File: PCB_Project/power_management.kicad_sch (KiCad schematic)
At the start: 0 parts

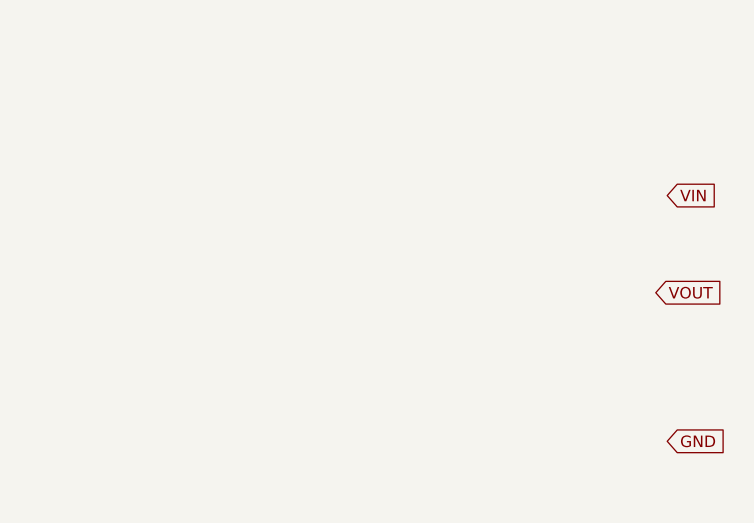
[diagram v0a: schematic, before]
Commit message: added power board
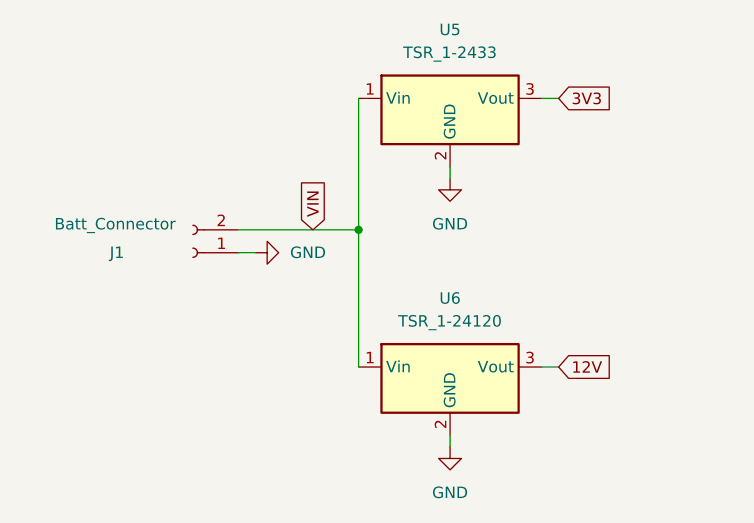
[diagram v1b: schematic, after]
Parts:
- added J1: Batt_Connector, symbol Connector:Conn_01x02_Socket
- added U5: TSR_1-2433, Converter_DCDC:Converter_DCDC_TRACO_TSR-1_THT, symbol Regulator_Switching:TSR_1-2433
- added U6: TSR_1-24120, Converter_DCDC:Converter_DCDC_TRACO_TSR-1_THT, symbol Regulator_Switching:TSR_1-24120
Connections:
- net GND: now also J1.1 (Pin_1), U5.2 (GND), U6.2 (GND)
- net VIN: now also J1.2 (Pin_2), U5.1 (Vin), U6.1 (Vin)
- new net 12V: U6.3 (Vout)
- new net 3V3: U5.3 (Vout)
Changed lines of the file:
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@@
 (kicad_sch (version 20230121) (generator eeschema)
   (paper "A4")
-  (global_label "VIN" (shape input) (at 144.145 64.135 0) (fields_autoplaced)
+  (junction (at 109.855 67.945) (diameter 0) (color 0 0 0 0)
+  )
+  (wire (pts (xy 120.015 60.96) (xy 120.015 62.23))
+    (stroke (width 0) (type default))
+  )
+  (wire (pts (xy 96.52 70.485) (xy 98.425 70.485))
+    (stroke (width 0) (type default))
+  )
+  (wire (pts (xy 96.52 67.945) (xy 109.855 67.945))
+    (stroke (width 0) (type default))
+  )
+  (wire (pts (xy 120.015 90.805) (xy 120.015 92.075))
+    (stroke (width 0) (type default))
+  )
+  (wire (pts (xy 130.175 53.34) (xy 132.08 53.34))
+    (stroke (width 0) (type default))
+  )
+  (wire (pts (xy 109.855 67.945) (xy 109.855 83.185))
+    (stroke (width 0) (type default))
+  )
+  (wire (pts (xy 130.175 83.185) (xy 132.08 83.185))
+    (stroke (width 0) (type default))
+  )
+  (wire (pts (xy 109.855 67.945) (xy 109.855 53.34))
+    (stroke (width 0) (type default))
+  )
+  (global_label "3V3" (shape input) (at 132.08 53.34 0) (fields_autoplaced)
     (effects (font (size 1.27 1.27)) (justify left))
-    (property "Intersheetrefs" "${INTERSHEET_REFS}" (at 150.0747 64.135 0)
+    (property "Intersheetrefs" "${INTERSHEET_REFS}" (at 138.4934 53.34 0)
       (effects (font (size 1.27 1.27)) (justify left) hide)
     )
   )
-  (global_label "GND" (shape input) (at 144.145 91.44 0) (fields_autoplaced)
+  (global_label "VIN" (shape input) (at 104.775 67.945 90) (fields_autoplaced)
     (effects (font (size 1.27 1.27)) (justify left))
-    (property "Intersheetrefs" "${INTERSHEET_REFS}" (at 150.9213 91.44 0)
+    (property "Intersheetrefs" "${INTERSHEET_REFS}" (at 104.775 62.0153 90)
       (effects (font (size 1.27 1.27)) (justify left) hide)
     )
   )
-  (global_label "VOUT" (shape input) (at 142.875 74.93 0) (fields_autoplaced)
+  (global_label "12V" (shape input) (at 132.08 83.185 0) (fields_autoplaced)
     (effects (font (size 1.27 1.27)) (justify left))
-    (property "Intersheetrefs" "${INTERSHEET_REFS}" (at 150.498 74.93 0)
+    (property "Intersheetrefs" "${INTERSHEET_REFS}" (at 138.4934 83.185 0)
       (effects (font (size 1.27 1.27)) (justify left) hide)
     )
   )
+  (symbol (lib_id "Regulator_Switching:TSR_1-24120") (at 120.015 85.725 0) (unit 1)
+    (in_bom yes) (on_board yes) (dnp no)
+    (property "Reference" "U6" (at 120.015 75.565 0)
+      (effects (font (size 1.27 1.27)))
+    )
+    (property "Value" "TSR_1-24120" (at 120.015 78.105 0)
+      (effects (font (size 1.27 1.27)))
+    )
+    (property "Footprint" "Converter_DCDC:Converter_DCDC_TRACO_TSR-1_THT" (at 120.015 89.535 0)
+      (effects (font (size 1.27 1.27) italic) (justify left) hide)
+    )
+    (property "Datasheet" "http://www.tracopower.com/products/tsr1.pdf" (at 120.015 85.725 0)
+      (effects (font (size 1.27 1.27)) hide)
+    )
+    (pin "1")
+    (pin "2")
+    (pin "3")
+    (instances
+      (project "PCB_Project"
+        (path "/3dbd20c6-0b48-4a74-89bd-dd4c54711bfb/c1270458-3028-4230-aa43-c8411af46874"
+          (reference "U6") (unit 1)
+        )
+      )
+    )
+  )
+  (symbol (lib_id "Regulator_Switching:TSR_1-2433") (at 120.015 55.88 0) (unit 1)
+    (in_bom yes) (on_board yes) (dnp no) (fields_autoplaced)
+    (property "Reference" "U5" (at 120.015 45.72 0)
+      (effects (font (size 1.27 1.27)))
+    )
+    (property "Value" "TSR_1-2433" (at 120.015 48.26 0)
+      (effects (font (size 1.27 1.27)))
+    )
+    (property "Footprint" "Converter_DCDC:Converter_DCDC_TRACO_TSR-1_THT" (at 120.015 59.69 0)
+      (effects (font (size 1.27 1.27) italic) (justify left) hide)
+    )
+    (property "Datasheet" "http://www.tracopower.com/products/tsr1.pdf" (at 120.015 55.88 0)
+      (effects (font (size 1.27 1.27)) hide)
+    )
+    (pin "1")
+    (pin "2")
+    (pin "3")
+    (instances
+      (project "PCB_Project"
+        (path "/3dbd20c6-0b48-4a74-89bd-dd4c54711bfb/c1270458-3028-4230-aa43-c8411af46874"
+          (reference "U5") (unit 1)
+        )
+      )
+    )
+  )
+  (symbol (lib_id "power:GND") (at 120.015 62.23 0) (unit 1)
+    (in_bom yes) (on_board yes) (dnp no) (fields_autoplaced)
+    (property "Reference" "#PWR012" (at 120.015 68.58 0)
+      (effects (font (size 1.27 1.27)) hide)
+    )
+    (property "Value" "GND" (at 120.015 67.31 0)
+      (effects (font (size 1.27 1.27)))
+    )
+    (property "Footprint" "" (at 120.015 62.23 0)
+      (effects (font (size 1.27 1.27)) hide)
+    )
+    (property "Datasheet" "" (at 120.015 62.23 0)
+      (effects (font (size 1.27 1.27)) hide)
+    )
+    (pin "1")
+    (instances
+      (project "PCB_Project"
+        (path "/3dbd20c6-0b48-4a74-89bd-dd4c54711bfb/c1270458-3028-4230-aa43-c8411af46874"
+          (reference "#PWR012") (unit 1)
+        )
+      )
+    )
+  )
+  (symbol (lib_id "power:GND") (at 120.015 92.075 0) (unit 1)
+    (in_bom yes) (on_board yes) (dnp no) (fields_autoplaced)
+    (property "Reference" "#PWR013" (at 120.015 98.425 0)
+      (effects (font (size 1.27 1.27)) hide)
+    )
+    (property "Value" "GND" (at 120.015 97.155 0)
+      (effects (font (size 1.27 1.27)))
+    )
+    (property "Footprint" "" (at 120.015 92.075 0)
+      (effects (font (size 1.27 1.27)) hide)
+    )
+    (property "Datasheet" "" (at 120.015 92.075 0)
+      (effects (font (size 1.27 1.27)) hide)
+    )
+    (pin "1")
+    (instances
+      (project "PCB_Project"
+        (path "/3dbd20c6-0b48-4a74-89bd-dd4c54711bfb/c1270458-3028-4230-aa43-c8411af46874"
+          (reference "#PWR013") (unit 1)
+        )
+      )
+    )
+  )
+  (symbol (lib_id "power:GND") (at 98.425 70.485 90) (unit 1)
+    (in_bom yes) (on_board yes) (dnp no)
+    (property "Reference" "#PWR011" (at 104.775 70.485 0)
+      (effects (font (size 1.27 1.27)) hide)
+    )
+    (property "Value" "GND" (at 102.235 70.485 90)
+      (effects (font (size 1.27 1.27)) (justify right))
+    )
+    (property "Footprint" "" (at 98.425 70.485 0)
+      (effects (font (size 1.27 1.27)) hide)
+    )
+    (property "Datasheet" "" (at 98.425 70.485 0)
+      (effects (font (size 1.27 1.27)) hide)
+    )
+    (pin "1")
+    (instances
+      (project "PCB_Project"
+        (path "/3dbd20c6-0b48-4a74-89bd-dd4c54711bfb/c1270458-3028-4230-aa43-c8411af46874"
+          (reference "#PWR011") (unit 1)
+        )
+      )
+    )
+  )
+  (symbol (lib_id "Connector:Conn_01x02_Socket") (at 91.44 70.485 180) (unit 1)
+    (in_bom yes) (on_board yes) (dnp no)
+    (property "Reference" "J1" (at 83.82 70.485 0)
+      (effects (font (size 1.27 1.27)) (justify left))
+    )
+    (property "Value" "Batt_Connector" (at 89.535 67.31 0)
+      (effects (font (size 1.27 1.27)) (justify left))
+    )
+    (property "Footprint" "" (at 91.44 70.485 0)
+      (effects (font (size 1.27 1.27)) hide)
+    )
+    (property "Datasheet" "~" (at 91.44 70.485 0)
+      (effects (font (size 1.27 1.27)) hide)
+    )
+    (pin "1")
+    (pin "2")
+    (instances
+      (project "PCB_Project"
+        (path "/3dbd20c6-0b48-4a74-89bd-dd4c54711bfb/c1270458-3028-4230-aa43-c8411af46874"
+          (reference "J1") (unit 1)
+        )
+      )
+    )
+  )

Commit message: done for the day work off this now
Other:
- moved on the sheet: J1, U5, U6
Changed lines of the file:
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@@
 (kicad_sch (version 20230121) (generator eeschema)
   (paper "A4")
-  (junction (at 109.855 67.945) (diameter 0) (color 0 0 0 0)
+  (junction (at 119.38 90.805) (diameter 0) (color 0 0 0 0)
   )
-  (wire (pts (xy 120.015 60.96) (xy 120.015 62.23))
+  (wire (pts (xy 129.54 83.82) (xy 129.54 85.09))
     (stroke (width 0) (type default))
   )
-  (wire (pts (xy 96.52 70.485) (xy 98.425 70.485))
+  (wire (pts (xy 106.045 93.345) (xy 107.95 93.345))
     (stroke (width 0) (type default))
   )
-  (wire (pts (xy 96.52 67.945) (xy 109.855 67.945))
+  (wire (pts (xy 106.045 90.805) (xy 119.38 90.805))
     (stroke (width 0) (type default))
   )
-  (wire (pts (xy 120.015 90.805) (xy 120.015 92.075))
+  (wire (pts (xy 129.54 113.665) (xy 129.54 114.935))
     (stroke (width 0) (type default))
   )
-  (wire (pts (xy 130.175 53.34) (xy 132.08 53.34))
+  (wire (pts (xy 139.7 76.2) (xy 141.605 76.2))
     (stroke (width 0) (type default))
   )
-  (wire (pts (xy 109.855 67.945) (xy 109.855 83.185))
+  (wire (pts (xy 119.38 90.805) (xy 119.38 106.045))
     (stroke (width 0) (type default))
   )
-  (wire (pts (xy 130.175 83.185) (xy 132.08 83.185))
+  (wire (pts (xy 139.7 106.045) (xy 141.605 106.045))
     (stroke (width 0) (type default))
   )
-  (wire (pts (xy 109.855 67.945) (xy 109.855 53.34))
+  (wire (pts (xy 119.38 90.805) (xy 119.38 76.2))
     (stroke (width 0) (type default))
   )
-  (global_label "3V3" (shape input) (at 132.08 53.34 0) (fields_autoplaced)
+  (global_label "3V3" (shape input) (at 141.605 76.2 0) (fields_autoplaced)
     (effects (font (size 1.27 1.27)) (justify left))
-    (property "Intersheetrefs" "${INTERSHEET_REFS}" (at 138.4934 53.34 0)
+    (property "Intersheetrefs" "${INTERSHEET_REFS}" (at 148.0184 76.2 0)
       (effects (font (size 1.27 1.27)) (justify left) hide)
     )
   )
-  (global_label "VIN" (shape input) (at 104.775 67.945 90) (fields_autoplaced)
+  (global_label "VIN" (shape input) (at 114.3 90.805 90) (fields_autoplaced)
     (effects (font (size 1.27 1.27)) (justify left))
-    (property "Intersheetrefs" "${INTERSHEET_REFS}" (at 104.775 62.0153 90)
+    (property "Intersheetrefs" "${INTERSHEET_REFS}" (at 114.3 84.8753 90)
       (effects (font (size 1.27 1.27)) (justify left) hide)
     )
   )
-  (global_label "12V" (shape input) (at 132.08 83.185 0) (fields_autoplaced)
+  (global_label "12V" (shape input) (at 141.605 106.045 0) (fields_autoplaced)
     (effects (font (size 1.27 1.27)) (justify left))
-    (property "Intersheetrefs" "${INTERSHEET_REFS}" (at 138.4934 83.185 0)
+    (property "Intersheetrefs" "${INTERSHEET_REFS}" (at 148.0184 106.045 0)
       (effects (font (size 1.27 1.27)) (justify left) hide)
     )
   )
-  (symbol (lib_id "Regulator_Switching:TSR_1-24120") (at 120.015 85.725 0) (unit 1)
+  (symbol (lib_id "Regulator_Switching:TSR_1-24120") (at 129.54 108.585 0) (unit 1)
     (in_bom yes) (on_board yes) (dnp no)
-    (property "Reference" "U6" (at 120.015 75.565 0)
+    (property "Reference" "U6" (at 129.54 98.425 0)
       (effects (font (size 1.27 1.27)))
     )
-    (property "Value" "TSR_1-24120" (at 120.015 78.105 0)
+    (property "Value" "TSR_1-24120" (at 129.54 100.965 0)
       (effects (font (size 1.27 1.27)))
     )
-    (property "Footprint" "Converter_DCDC:Converter_DCDC_TRACO_TSR-1_THT" (at 120.015 89.535 0)
+    (property "Footprint" "Converter_DCDC:Converter_DCDC_TRACO_TSR-1_THT" (at 129.54 112.395 0)
       (effects (font (size 1.27 1.27) italic) (justify left) hide)
     )
-    (property "Datasheet" "http://www.tracopower.com/products/tsr1.pdf" (at 120.015 85.725 0)
+    (property "Datasheet" "http://www.tracopower.com/products/tsr1.pdf" (at 129.54 108.585 0)
       (effects (font (size 1.27 1.27)) hide)
     )
@@
     )
   )
-  (symbol (lib_id "Regulator_Switching:TSR_1-2433") (at 120.015 55.88 0) (unit 1)
+  (symbol (lib_id "Regulator_Switching:TSR_1-2433") (at 129.54 78.74 0) (unit 1)
     (in_bom yes) (on_board yes) (dnp no) (fields_autoplaced)
-    (property "Reference" "U5" (at 120.015 45.72 0)
+    (property "Reference" "U5" (at 129.54 68.58 0)
       (effects (font (size 1.27 1.27)))
     )
-    (property "Value" "TSR_1-2433" (at 120.015 48.26 0)
+    (property "Value" "TSR_1-2433" (at 129.54 71.12 0)
       (effects (font (size 1.27 1.27)))
     )
-    (property "Footprint" "Converter_DCDC:Converter_DCDC_TRACO_TSR-1_THT" (at 120.015 59.69 0)
+    (property "Footprint" "Converter_DCDC:Converter_DCDC_TRACO_TSR-1_THT" (at 129.54 82.55 0)
       (effects (font (size 1.27 1.27) italic) (justify left) hide)
     )
-    (property "Datasheet" "http://www.tracopower.com/products/tsr1.pdf" (at 120.015 55.88 0)
+    (property "Datasheet" "http://www.tracopower.com/products/tsr1.pdf" (at 129.54 78.74 0)
       (effects (font (size 1.27 1.27)) hide)
     )
@@
     )
   )
-  (symbol (lib_id "power:GND") (at 120.015 62.23 0) (unit 1)
+  (symbol (lib_id "power:GND") (at 129.54 85.09 0) (unit 1)
     (in_bom yes) (on_board yes) (dnp no) (fields_autoplaced)
-    (property "Reference" "#PWR012" (at 120.015 68.58 0)
+    (property "Reference" "#PWR012" (at 129.54 91.44 0)
       (effects (font (size 1.27 1.27)) hide)
     )
-    (property "Value" "GND" (at 120.015 67.31 0)
+    (property "Value" "GND" (at 129.54 90.17 0)
       (effects (font (size 1.27 1.27)))
     )
-    (property "Footprint" "" (at 120.015 62.23 0)
+    (property "Footprint" "" (at 129.54 85.09 0)
       (effects (font (size 1.27 1.27)) hide)
     )
-    (property "Datasheet" "" (at 120.015 62.23 0)
+    (property "Datasheet" "" (at 129.54 85.09 0)
       (effects (font (size 1.27 1.27)) hide)
     )
@@
     )
   )
-  (symbol (lib_id "power:GND") (at 120.015 92.075 0) (unit 1)
+  (symbol (lib_id "power:GND") (at 129.54 114.935 0) (unit 1)
     (in_bom yes) (on_board yes) (dnp no) (fields_autoplaced)
-    (property "Reference" "#PWR013" (at 120.015 98.425 0)
+    (property "Reference" "#PWR013" (at 129.54 121.285 0)
       (effects (font (size 1.27 1.27)) hide)
     )
-    (property "Value" "GND" (at 120.015 97.155 0)
+    (property "Value" "GND" (at 129.54 120.015 0)
       (effects (font (size 1.27 1.27)))
     )
-    (property "Footprint" "" (at 120.015 92.075 0)
+    (property "Footprint" "" (at 129.54 114.935 0)
       (effects (font (size 1.27 1.27)) hide)
     )
-    (property "Datasheet" "" (at 120.015 92.075 0)
+    (property "Datasheet" "" (at 129.54 114.935 0)
       (effects (font (size 1.27 1.27)) hide)
     )
@@
     )
   )
-  (symbol (lib_id "power:GND") (at 98.425 70.485 90) (unit 1)
+  (symbol (lib_id "power:GND") (at 107.95 93.345 90) (unit 1)
     (in_bom yes) (on_board yes) (dnp no)
-    (property "Reference" "#PWR011" (at 104.775 70.485 0)
+    (property "Reference" "#PWR011" (at 114.3 93.345 0)
       (effects (font (size 1.27 1.27)) hide)
     )
-    (property "Value" "GND" (at 102.235 70.485 90)
+    (property "Value" "GND" (at 111.76 93.345 90)
       (effects (font (size 1.27 1.27)) (justify right))
     )
-    (property "Footprint" "" (at 98.425 70.485 0)
+    (property "Footprint" "" (at 107.95 93.345 0)
       (effects (font (size 1.27 1.27)) hide)
     )
-    (property "Datasheet" "" (at 98.425 70.485 0)
+    (property "Datasheet" "" (at 107.95 93.345 0)
       (effects (font (size 1.27 1.27)) hide)
     )
@@
     )
   )
-  (symbol (lib_id "Connector:Conn_01x02_Socket") (at 91.44 70.485 180) (unit 1)
+  (symbol (lib_id "Connector:Conn_01x02_Socket") (at 100.965 93.345 180) (unit 1)
     (in_bom yes) (on_board yes) (dnp no)
-    (property "Reference" "J1" (at 83.82 70.485 0)
+    (property "Reference" "J1" (at 93.345 93.345 0)
       (effects (font (size 1.27 1.27)) (justify left))
     )
-    (property "Value" "Batt_Connector" (at 89.535 67.31 0)
+    (property "Value" "Batt_Connector" (at 99.06 90.17 0)
       (effects (font (size 1.27 1.27)) (justify left))
     )
-    (property "Footprint" "" (at 91.44 70.485 0)
+    (property "Footprint" "" (at 100.965 93.345 0)
       (effects (font (size 1.27 1.27)) hide)
     )
-    (property "Datasheet" "~" (at 91.44 70.485 0)
+    (property "Datasheet" "~" (at 100.965 93.345 0)
       (effects (font (size 1.27 1.27)) hide)
     )

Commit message: ignore how ugly it looks I need to fix it
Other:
- moved on the sheet: U6

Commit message: 2 footprints left then can design
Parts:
- J1: footprint (none) -> Connector_JST:JST_PH_B2B-PH-K_1x02_P2.00mm_Vertical
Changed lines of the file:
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@@
 			)
 		)
-		(property "Footprint" ""
+		(property "Footprint" "Connector_JST:JST_PH_B2B-PH-K_1x02_P2.00mm_Vertical"
 			(at 100.965 93.345 0)
 			(effects

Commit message: working on final board
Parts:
- removed J1: Batt_Connector, Connector_JST:JST_PH_B2B-PH-K_1x02_P2.00mm_Vertical, symbol Connector:Conn_01x02_Socket
- removed U5: TSR_1-2433, Converter_DCDC:Converter_DCDC_TRACO_TSR-1_THT, symbol Regulator_Switching:TSR_1-2433
- removed U6: TSR_1-24120, Converter_DCDC:Converter_DCDC_TRACO_TSR-1_THT, symbol Regulator_Switching:TSR_1-24120
- added C13: 10nF, symbol Device:C
- added C14, C19: C_Polarized, symbol Device:C_Polarized_US
- added C15, C16, C20, C21: C, symbol Device:C
- added C17: 180µF, symbol Device:C_Polarized_US
- added C18: nF, symbol Device:C
- added C22: C, symbol Device:C_Polarized_US
- added D1, D2: D_Schottky, symbol Device:D_Schottky
- added J6: Batt_Connector, Connector_JST:JST_PH_B2B-PH-K_1x02_P2.00mm_Vertical, symbol Connector:Conn_01x02_Socket
- added L1: 4.7µH, symbol Device:L
- added L2: 3.6µH, symbol Device:L
- added R14, R16: 1kR, symbol Device:R
- added R15: 1.54k, symbol Device:R
- added U10: LM22678TJ-5, Package_TO_SOT_SMD:TO-263-7_TabPin8, symbol Regulator_Switching:LM22678TJ-5
- added U9: LM22678TJ-ADJ, Package_TO_SOT_SMD:TO-263-7_TabPin8, symbol Regulator_Switching:LM22678TJ-ADJ
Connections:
- net GND: now also C14.2, C15.2, C16.2, C17.2, C19.2, C20.2, C21.2, C22.2, D1.2 (A), D2.2 (A), J6.1 (Pin_1), R14.2, R16.2, U10.4 (GND), U10.8 (GND), U9.4 (GND), U9.8 (GND)
- new net: C18.1, U10.3 (BOOT)
- new net: C18.2, D2.1 (K), L2.1, U10.1 (SW)
- new net: C13.2, D1.1 (K), L1.1, U9.1 (SW)
- new net: C13.1, U9.3 (BOOT)
- new net: R14.1, R15.2, U9.6 (FB)
- new net +3.3V: C17.1, C22.1, L1.2, L2.2, R15.1, R16.1, U10.6 (FB)
- new net BATT_V: C14.1, C15.1, C16.1, C19.1, C20.1, C21.1, J6.2 (Pin_2), U10.2 (VIN), U9.2 (VIN)
- no-connect marks 0 -> 2
